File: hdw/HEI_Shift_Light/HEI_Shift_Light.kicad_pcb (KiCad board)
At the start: 4 copper layers, 70.7 x 56.9 mm, 111 parts, among them J201 VIN, J401 TACH, J501 PICKIT4, J601 USB_C_Receptacle_USB2.0_16P, Q301 DMN3150LW-7, Q302 DMN3150LW-7, Q701 DMN3150LW-7, Q702 DMN3150LW-7, Q703 DMN3150LW-7, U201 TPS26624DRCR, U301 TPS62153, U401 LM2907, U402 MCP4019-103ELT, U501 PIC18F16Q41, U601 FT234XD, U602 ISO7321C

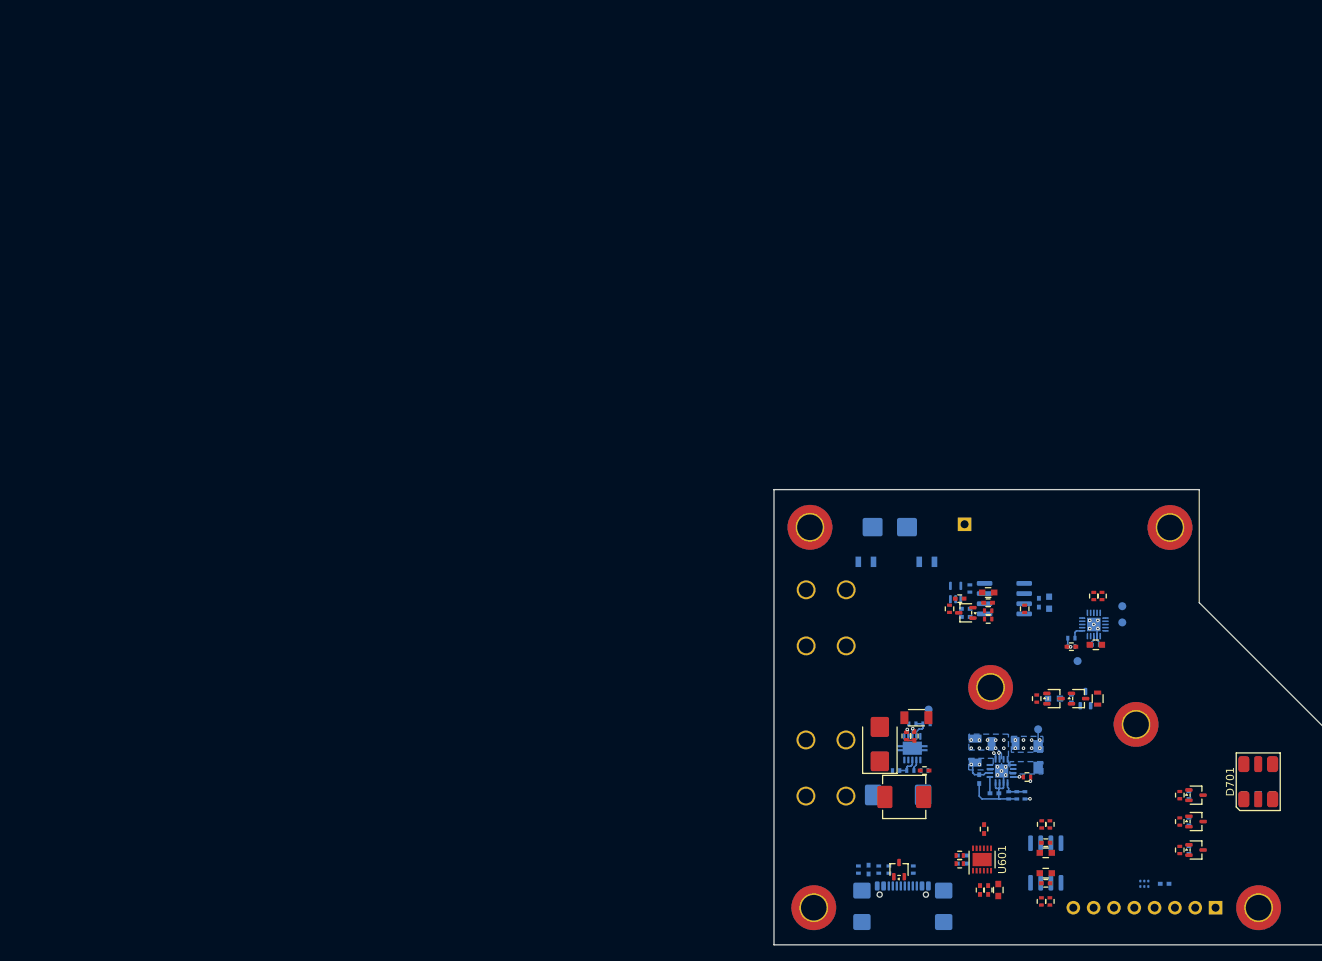
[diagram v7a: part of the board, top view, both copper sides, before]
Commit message: routed most of board
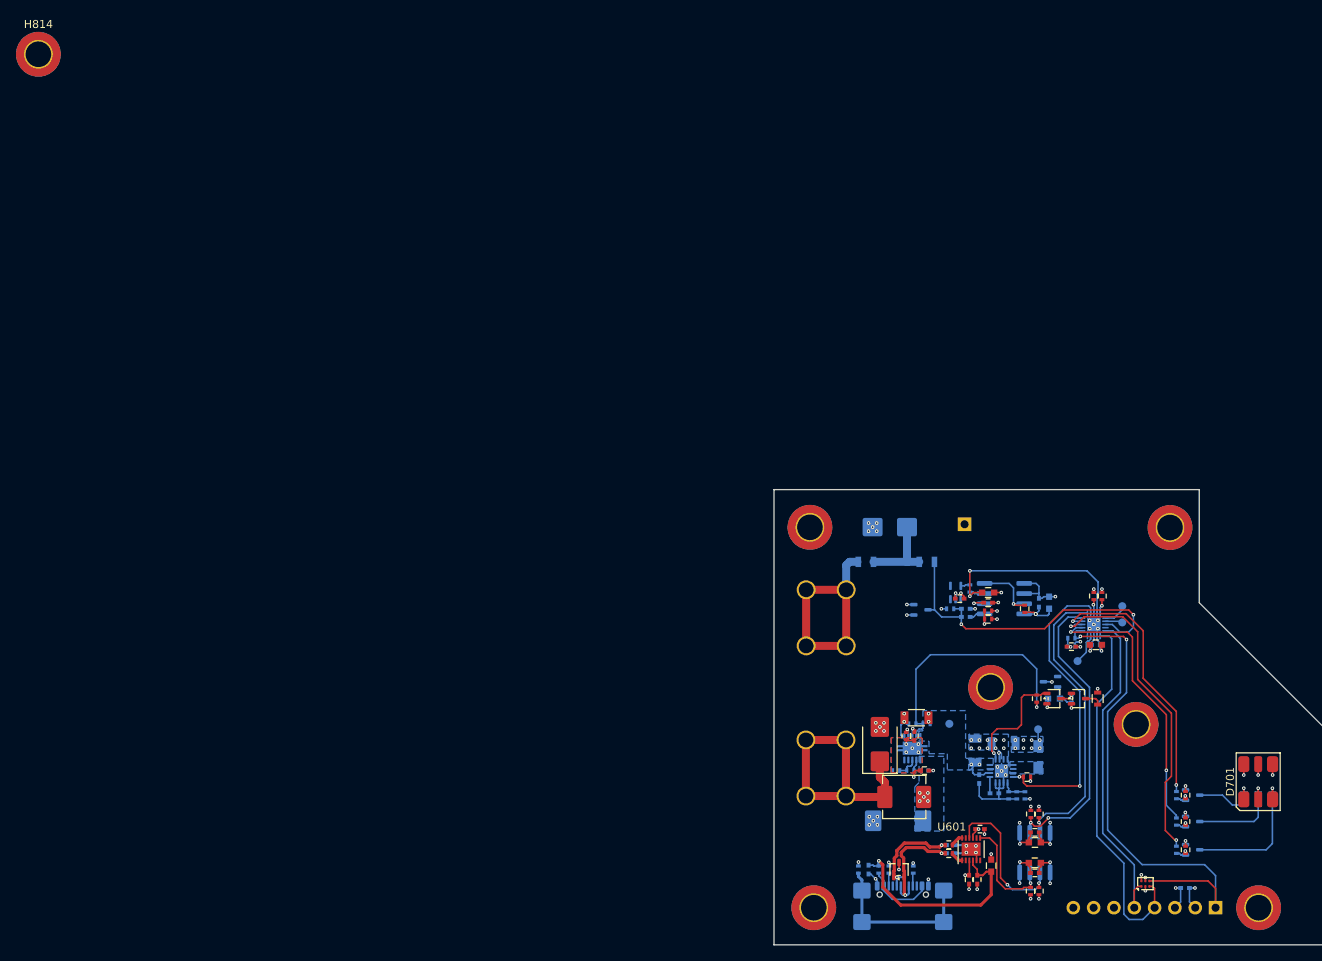
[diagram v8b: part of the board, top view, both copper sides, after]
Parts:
- added H814: MountingHole_Pad, MountingHole:MountingHole_3.2mm_M3_DIN965_Pad_TopBottom, F.Cu at (3.08, 3.08)
- D402, Q701, Q702, Q703, R403, R701, R702, R703: moved to B.Cu
- D501, R704, R705, R706: moved to F.Cu
- moved D402 5.62 mm to (113.4, 72.5), turned to 0 degrees
- moved D301 4.85 mm to (129.6, 81.5), turned to 180 degrees
- moved C201 3.23 mm to (110.5, 98.9)
- moved C603 3.18 mm to (122.2, 104.5), turned to 90 degrees
- moved TP202 3.14 mm to (116.9, 86.8)
- moved C501 2.60 mm to (146.4, 107.3)
- moved C602 1.88 mm to (120.4, 106.2)
- moved R602 1.88 mm to (127.1, 98.0)
- moved U601 1.88 mm to (119.7, 102.4)
- moved C604 1.88 mm to (119.4, 106.2)
- moved C607 1.88 mm to (117.1, 101.9)
- moved C608 1.88 mm to (117.1, 102.9)
- moved R601 1.88 mm to (128.1, 98.0)
- moved R603 1.88 mm to (116.9, 101.9)
- moved R604 1.88 mm to (116.9, 102.9)
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- renumbered H814 to H804
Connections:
- D501 pad 1: +5V -> PIC18F_ICSPCLK
- D501 pad 3: ~{PIC18F_MCLR} -> PIC18F_ICSPDAT
- D501 pad 4: PIC18F_ICSPDAT -> ~{PIC18F_MCLR}
- D501 pad 6: PIC18F_ICSPCLK -> +5V
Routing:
- net ~{PIC18F_MCLR}: track 1.71 -> 64.1 mm, vias 0 -> 2
- net PIC18F_ICSPDAT: track 0.00 -> 46.1 mm
- net TACH_PULSE: track 0.00 -> 42.1 mm, vias 0 -> 2
- net PIC18F_ICSPCLK: track 0.00 -> 41.7 mm
- net LED_G: track 0.00 -> 40.7 mm, vias 0 -> 2
- net USB_UART_RX: track 0.00 -> 37.6 mm, vias 0 -> 2
- net USB_UART_TX: track 0.00 -> 37.1 mm, vias 0 -> 1
- net POS5_PGOOD: track 1.28 -> 37.9 mm, vias 1 -> 2
- net LED_R: track 0.00 -> 34.5 mm, vias 0 -> 2
- net GND: track 15.5 -> 49.8 mm, vias 20 -> 59
- net /Input Power/VIN_BATT: track 0.00 -> 33.6 mm
- net LED_B: track 0.00 -> 33.1 mm, vias 0 -> 2
- net +5V: track 5.31 -> 35.7 mm, vias 11 -> 30
- net VIN_PGOOD: track 3.02 -> 31.8 mm, vias 0 -> 1
- net /Input Signal/TACH_IN: track 0.00 -> 28.7 mm
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- added copper zone on In2.Cu, net +3.3V_USB
- added copper zone on In2.Cu, net +5V
- added copper zone on B.Cu, net /Input Power/VIN_FILT
- added copper zone on In1.Cu, net GND
- added copper zone on In1.Cu, net GND_USB
- added copper zone on B.Cu, net Net-(U201-PAD)
- added copper zone on F.Cu, net Net-(U201-PAD)
